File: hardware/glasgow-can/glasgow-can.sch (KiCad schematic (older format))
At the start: 6 parts, among them J1 Conn_02x10_Odd_Even, J2 A-DS 09 A/KG-T2S, J3 Conn_01x09_Male, J4 Conn_01x03_Male, J5 Conn_02x10_Odd_Even, J6 Conn_01x03

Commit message: tidy up schematics
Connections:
- net labels added: CAN1_SILENT, CAN2_SILENT
- net labels removed: CAN1_S, CAN2_S
- wire segments 82 -> 85
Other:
- note added: "CAN1 allows you to connect an arbitary DE-9 cable to the CAN interface.\nThe patching between J3 and J4 provide flexibility, as there doesn't appear\nto be a single DE-9 pinout for CAN - the OBD-II cables have one pinout,\nand each vendor appears to have their own (Peak, NI, etc...)"
- note added: "CAN2 breaks out to a 3-way spring-loaded terminal block. This permits\nthe user to connect any bare-wire cable, in any way they wish."
- note added: "Glasgow Interface\nPort A"
- note added: "Glasgow Interface\nPort B"
- note added: "NOTE: Label these pins clearly on Top Silk\n\nBosch / Vector / Intrepid Control Systems use:\npin 3 = 0v\npin 2 = CANL\npin 7 = CANH"
- note removed: "Port A"
- note removed: "Port B"
- moved on the sheet: J1, J2, J3, J4, J5, J6

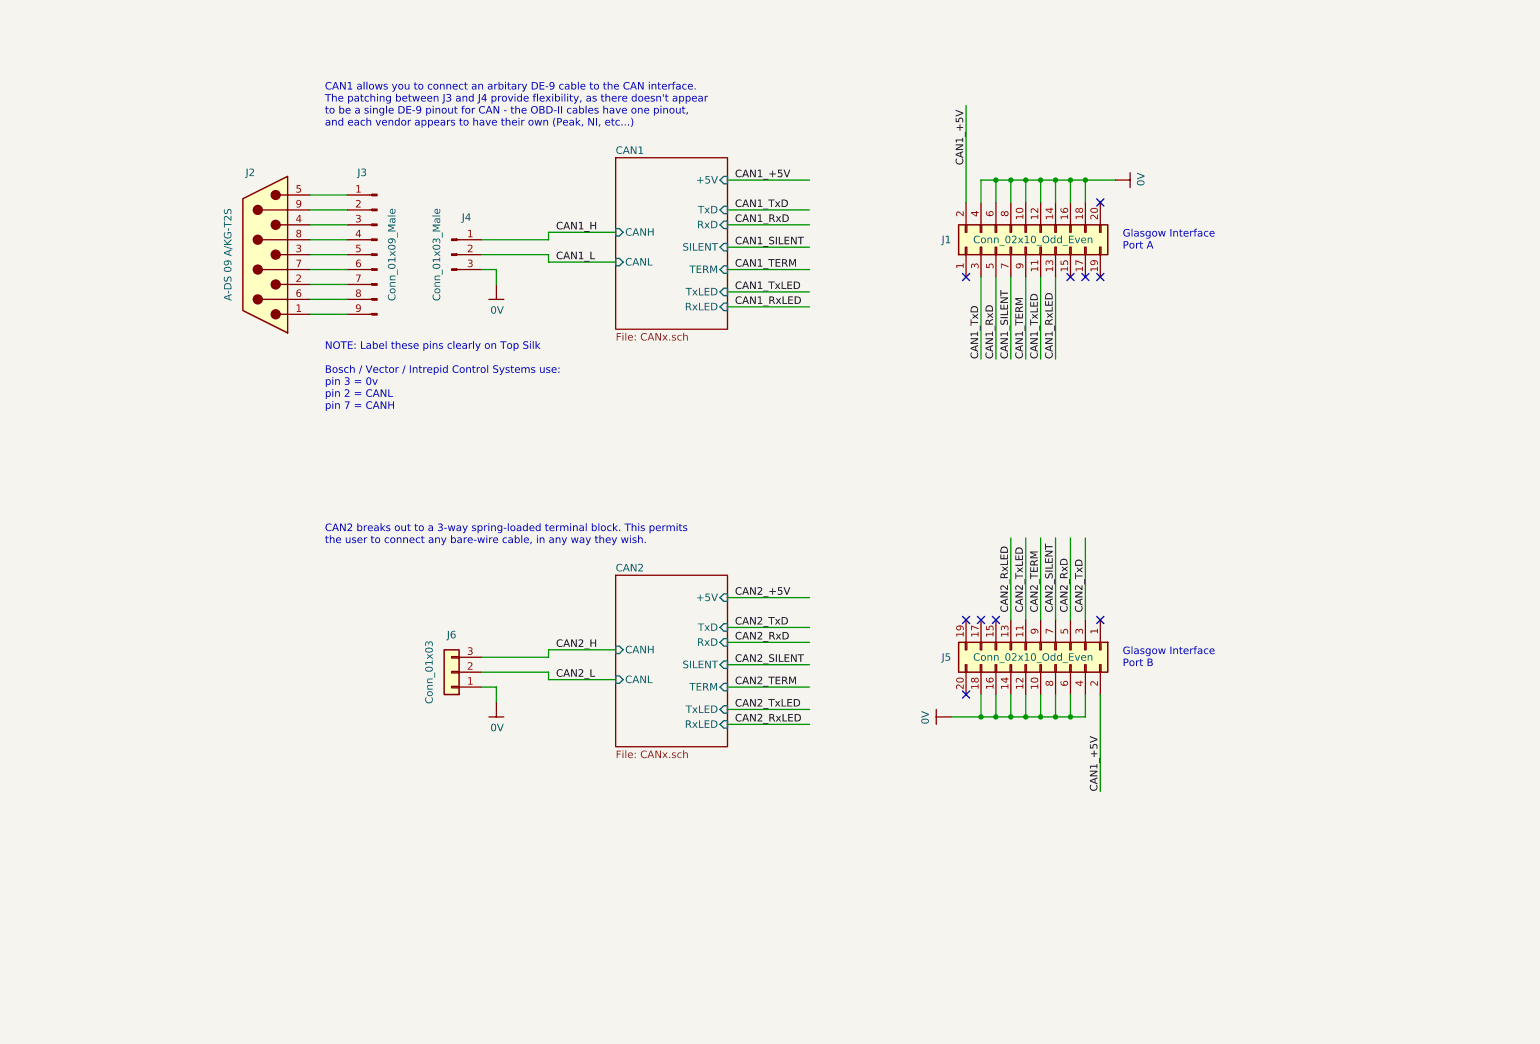
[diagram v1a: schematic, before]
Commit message: add note about pinouts via CANtact / Linklayer wiki
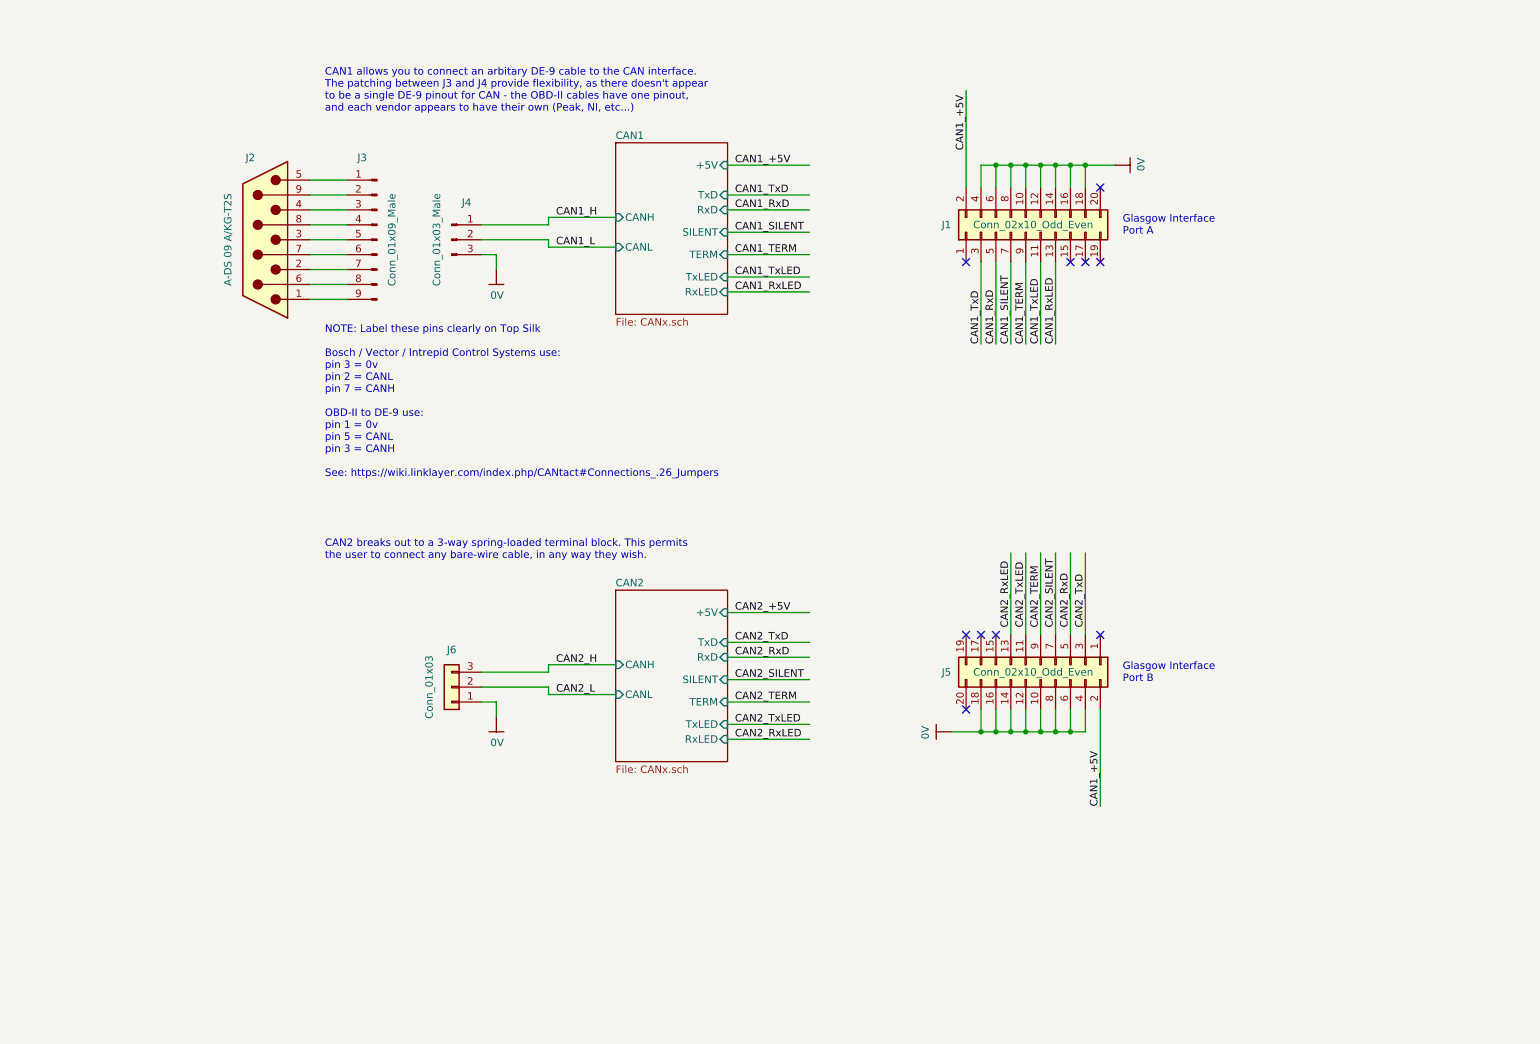
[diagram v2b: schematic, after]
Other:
- note added: "NOTE: Label these pins clearly on Top Silk\n\nBosch / Vector / Intrepid Control Systems use:\npin 3 = 0v\npin 2 = CANL\npin 7 = CANH\n\nOBD-II to DE-9 use:\npin 1 = 0v\npin 5 = CANL\npin 3 = CANH\n\nSee: https://wiki.linklayer.com/index.php/CANtact#Connections_.26_Jumpers"
- note removed: "NOTE: Label these pins clearly on Top Silk\n\nBosch / Vector / Intrepid Control Systems use:\npin 3 = 0v\npin 2 = CANL\npin 7 = CANH"
- moved on the sheet: J1, J2, J3, J4, J5, J6

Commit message: schematic revised according to discussion in #1, and layout mostly complete... some TODOs remain
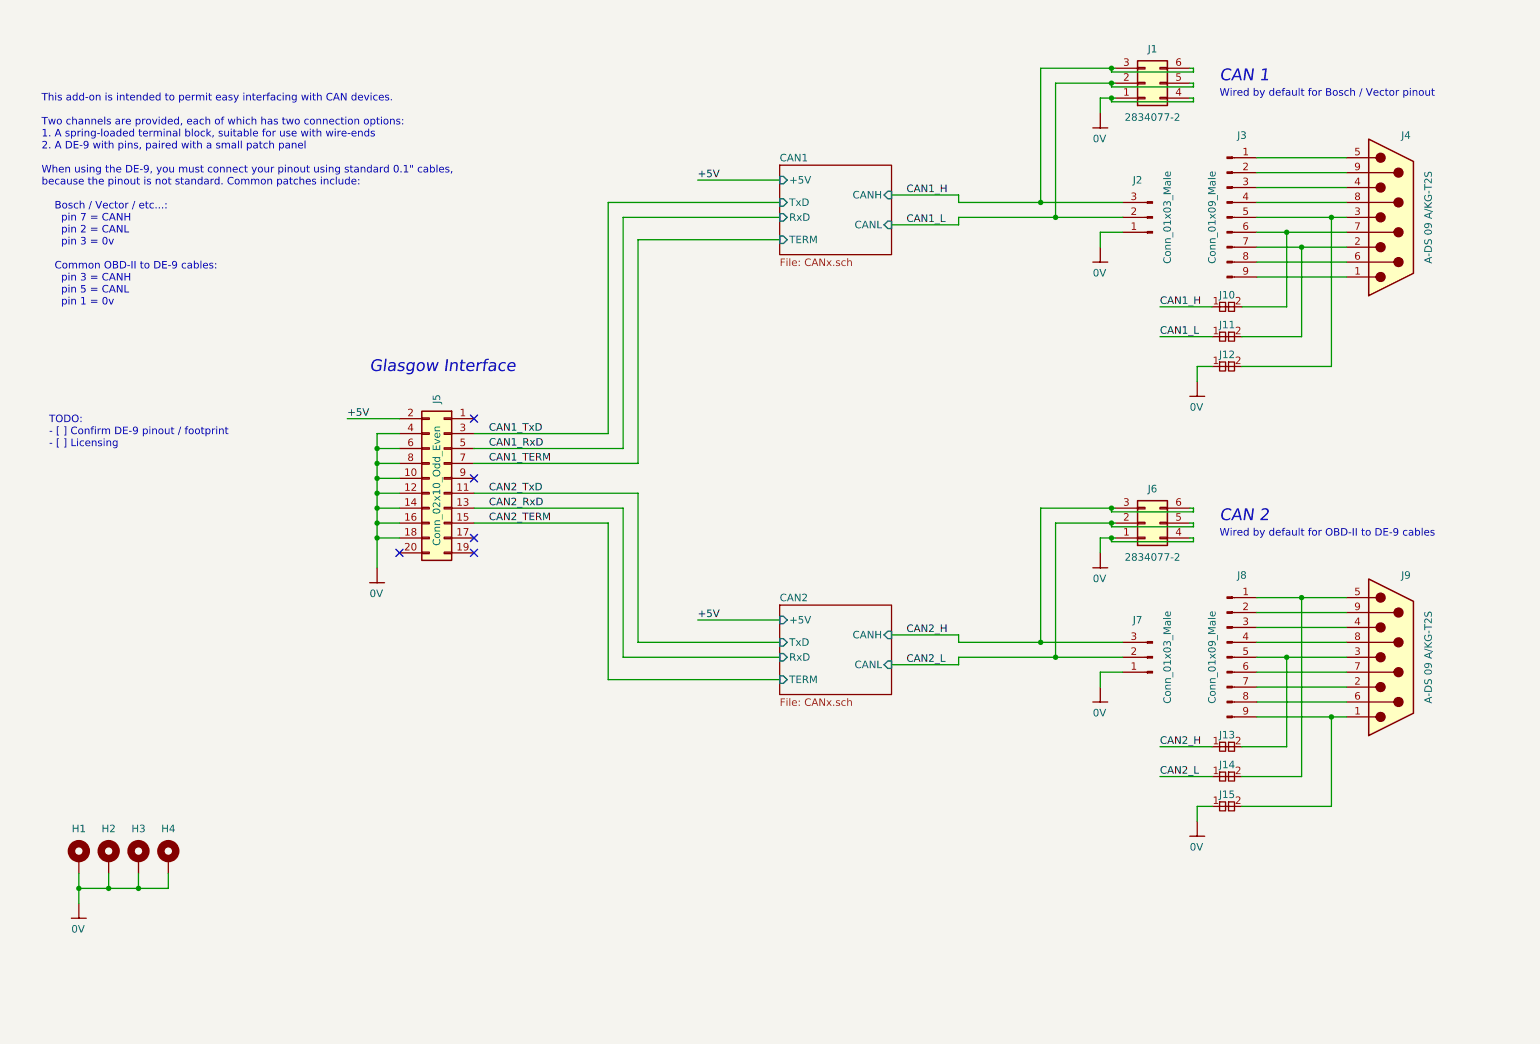
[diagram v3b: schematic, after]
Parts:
- removed J2: A-DS 09 A/KG-T2S, Connector_Dsub:DSUB-9_Female_Horizontal_P2.77x2.84mm_EdgePinOffset7.70mm_Housed_MountingHolesOffset9.12mm, symbol Connector:DB9_Male
- removed J5: Conn_02x10_Odd_Even, Connector_PinSocket_2.54mm:PinSocket_2x10_P2.54mm_Vertical_SMD, symbol Connector_Generic:Conn_02x10_Odd_Even
- removed J6: Conn_01x03, glasgow-can:TE_2834077-2, symbol Connector_Generic:Conn_01x03
- added H1, H2, H3, H4: MountingHole_Pad, MountingHole:MountingHole_3.2mm_M3_Pad_Via, symbol Mechanical:MountingHole_Pad
- added J1, J6: 2834077-2, glasgow-can:TE_2834077-2, symbol Connector_Generic:Conn_02x03_Top_Bottom
- added J10, J11, J12, J13, J14, J15: pkl_jumper_nc, pkl_jumpers:J_NC_0603_20, symbol pkl_misc:pkl_jumper_nc
- added J4, J9: A-DS 09 A/KG-T2S, Connector_Dsub:DSUB-9_Female_Horizontal_P2.77x2.84mm_EdgePinOffset7.70mm_Housed_MountingHolesOffset9.12mm, symbol Connector:DB9_Male
- added J7: Conn_01x03_Male, Connector_PinHeader_2.54mm:PinHeader_1x03_P2.54mm_Vertical, symbol Connector:Conn_01x03_Male
- added J8: Conn_01x09_Male, Connector_PinHeader_2.54mm:PinHeader_1x09_P2.54mm_Vertical, symbol Connector:Conn_01x09_Male
- J5: renamed from J1; footprint Connector_PinSocket_2.54mm:PinSocket_2x10_P2.54mm_Vertical_SMD -> Connector_IDC:IDC-Header_2x10_P2.54mm_Vertical
- renumbered J4 to J2
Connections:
- net labels added: +5V
- net labels removed: CAN1_+5V, CAN1_RxLED, CAN1_SILENT, CAN1_TxLED, CAN2_+5V, CAN2_RxLED, CAN2_SILENT, CAN2_TxLED
- wire segments 85 -> 151
- no-connect marks 10 -> 5
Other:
- note added: "CAN 1"
- note added: "CAN 2"
- note added: "Glasgow Interface"
- note added: "TODO:\n- [ ] Confirm DE-9 pinout / footprint\n- [ ] Licensing"
- note added: "This add-on is intended to permit easy interfacing with CAN devices.\n\nTwo channels are provided, each of which has two connection options:\n1. A spring-loaded terminal block, suitable for use with wire-ends\n2. A DE-9 with pins, paired with a small patch panel\n\nWhen using the DE-9, you must connect your pinout using standard 0.1" cables,\nbecause the pinout is not standard. Common patches inc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"
- note added: "Wired by default for Bosch / Vector pinout"
- note added: "Wired by default for OBD-II to DE-9 cables"
- note removed: "CAN1 allows you to connect an arbitary DE-9 cable to the CAN interface.\nThe patching between J3 and J4 provide flexibility, as there doesn't appear\nto be a single DE-9 pinout for CAN - the OBD-II cables have one pinout,\nand each vendor appears to have their own (Peak, NI, etc...)"
- note removed: "CAN2 breaks out to a 3-way spring-loaded terminal block. This permits\nthe user to connect any bare-wire cable, in any way they wish."
- note removed: "Glasgow Interface\nPort A"
- note removed: "Glasgow Interface\nPort B"
- note removed: "NOTE: Label these pins clearly on Top Silk\n\nBosch / Vector / Intrepid Control Systems use:\npin 3 = 0v\npin 2 = CANL\npin 7 = CANH\n\nOBD-II to DE-9 use:\npin 1 = 0v\npin 5 = CANL\npin 3 = CANH\n\nSee: https://wiki.linklayer.com/index.php/CANtact#Connections_.26_Jumpers"
- moved on the sheet: J2, J5
